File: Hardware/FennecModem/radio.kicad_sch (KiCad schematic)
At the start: 12 parts, among them J201 Conn_Coaxial, U201 DRA818V

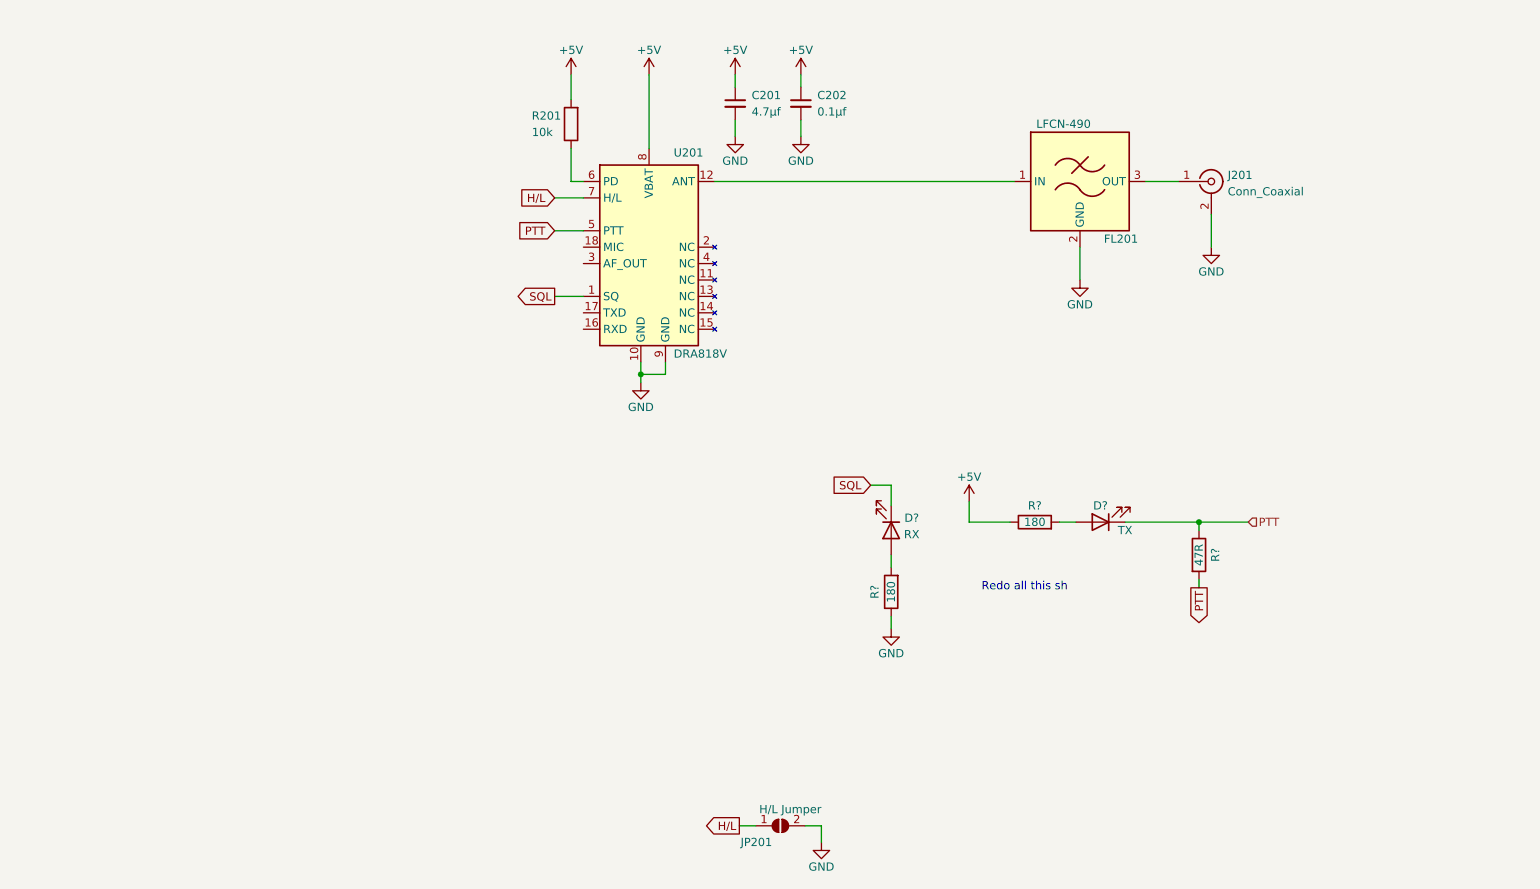
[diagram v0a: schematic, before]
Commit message: Add modem components, bump edge card connector in upstream
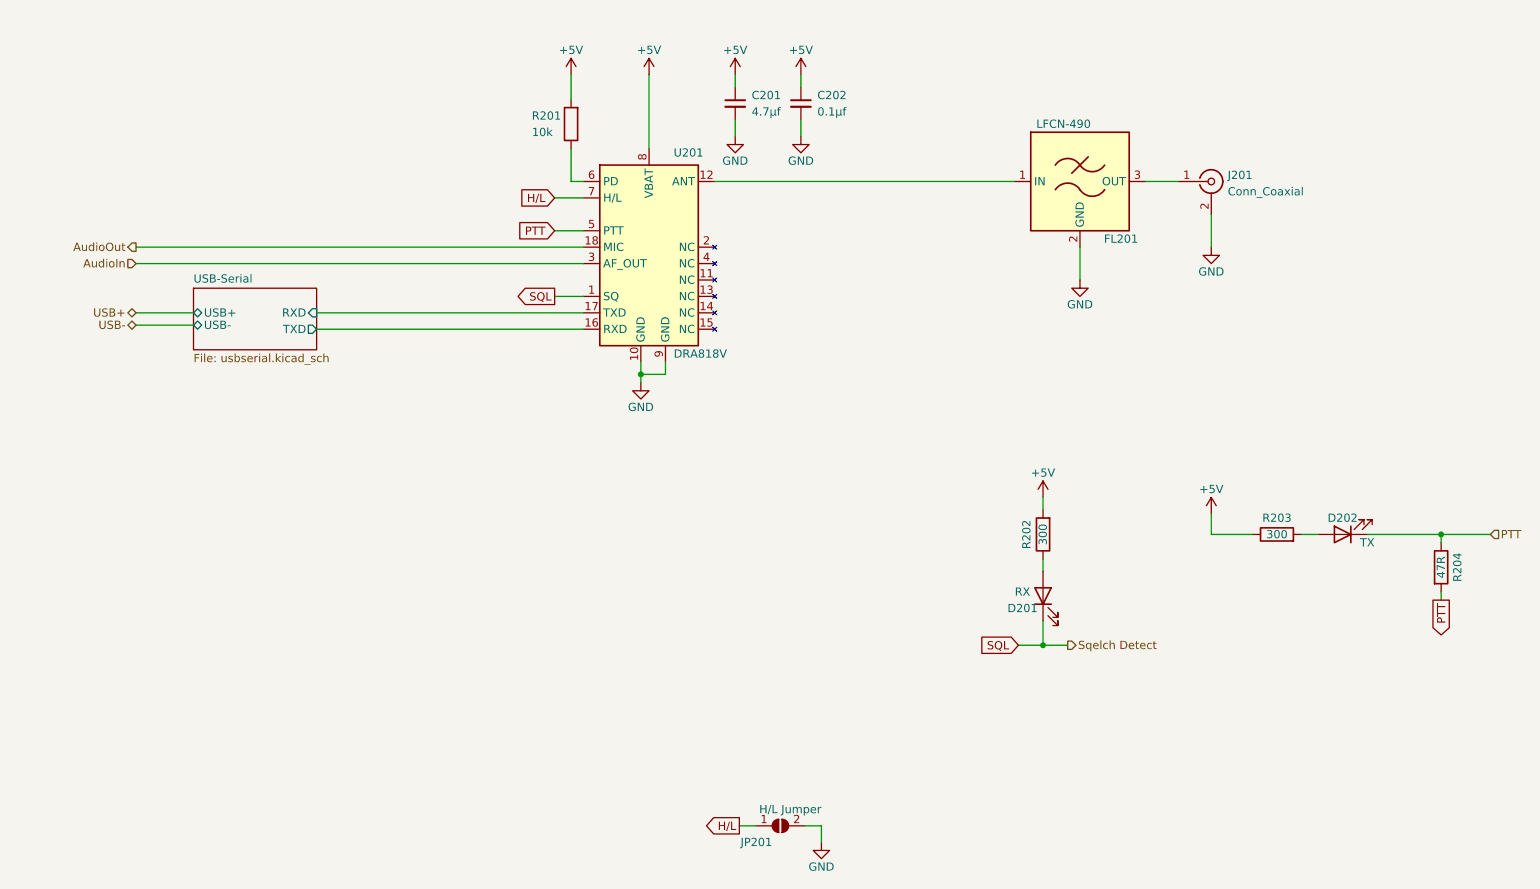
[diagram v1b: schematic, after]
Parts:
- removed D?: RX, LED_SMD:LED_0603_1608Metric, symbol Device:LED
- removed R?: 180, Resistor_SMD:R_0805_2012Metric, symbol Device:R
- added D201: RX, LED_SMD:LED_0603_1608Metric, symbol Device:LED
- added R202: 300, Resistor_SMD:R_0805_2012Metric, symbol Device:R
- R203: renamed from R?; value 180 -> 300
- gave numbers to parts that had none: 2
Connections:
- net +5V: now also R202.2
- net SQL: now also D201.1 (K)
- net USB-Serial/TXD: now reaches U201.16 (RXD)
- net USB-Serial/RXD: now reaches U201.17 (TXD)
- net AudioOut: now reaches U201.18 (MIC)
- net AudioIn: now reaches U201.3 (AF_OUT)
- new net: D201.2 (A), R202.1
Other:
- added sheet USB-Serial (usbserial.kicad_sch)
- note removed: "Redo all this sh"
- moved on the sheet: D202, R203, R204

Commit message: F*ck yeah edge connectors!
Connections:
- net USB-Serial/RXD renamed TXD
- net USB-Serial/TXD renamed RXD
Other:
- removed sheet USB-Serial
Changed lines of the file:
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@@
     (stroke (width 0) (type default) (color 0 0 0 0))
   )
-  (wire (pts (xy 94.615 109.22) (xy 135.89 109.22))
+  (wire (pts (xy 120.015 109.22) (xy 135.89 109.22))
     (stroke (width 0) (type default) (color 0 0 0 0))
   )
@@
     (stroke (width 0) (type default) (color 0 0 0 0))
   )
-  (wire (pts (xy 94.615 111.76) (xy 135.89 111.76))
-    (stroke (width 0) (type default) (color 0 0 0 0))
-  )
-  (wire (pts (xy 66.675 109.22) (xy 75.565 109.22))
+  (wire (pts (xy 120.015 111.76) (xy 135.89 111.76))
     (stroke (width 0) (type default) (color 0 0 0 0))
   )
@@
     (stroke (width 0) (type default) (color 0 0 0 0))
   )
-  (wire (pts (xy 66.675 99.06) (xy 135.89 99.06))
+  (wire (pts (xy 120.015 99.06) (xy 135.89 99.06))
     (stroke (width 0) (type default) (color 0 0 0 0))
   )
@@
     (stroke (width 0) (type default) (color 0 0 0 0))
   )
-  (wire (pts (xy 135.89 101.6) (xy 66.675 101.6))
+  (wire (pts (xy 135.89 101.6) (xy 120.015 101.6))
     (stroke (width 0) (type default) (color 0 0 0 0))
   )
@@
     (stroke (width 0) (type default) (color 0 0 0 0))
   )
-  (wire (pts (xy 66.675 111.125) (xy 75.565 111.125))
-    (stroke (width 0) (type default) (color 0 0 0 0))
-  )
   (wire (pts (xy 247.015 143.51) (xy 249.555 143.51))
     (stroke (width 0) (type default) (color 0 0 0 0))
@@
     )
   )
-  (hierarchical_label "AudioIn" (shape input) (at 66.675 101.6 180)
-    (effects (font (size 1.27 1.27)) (justify right))
-  )
-  (hierarchical_label "AudioOut" (shape output) (at 66.675 99.06 180)
-    (effects (font (size 1.27 1.27)) (justify right))
-  )
-  (hierarchical_label "USB-" (shape bidirectional) (at 66.675 111.125 180)
+  (hierarchical_label "AudioIn" (shape input) (at 120.015 101.6 180)
+    (effects (font (size 1.27 1.27)) (justify right))
+  )
+  (hierarchical_label "AudioOut" (shape output) (at 120.015 99.06 180)
+    (effects (font (size 1.27 1.27)) (justify right))
+  )
+  (hierarchical_label "TXD" (shape output) (at 120.015 109.22 180)
     (effects (font (size 1.27 1.27)) (justify right))
   )
@@
     (effects (font (size 1.27 1.27)) (justify left))
   )
-  (hierarchical_label "USB+" (shape bidirectional) (at 66.675 109.22 180)
-    (effects (font (size 1.27 1.27)) (justify right))
-  )
   (hierarchical_label "Sqelch Detect" (shape output) (at 210.82 160.655 0)
     (effects (font (size 1.27 1.27)) (justify left))
+  )
+  (hierarchical_label "RXD" (shape input) (at 120.015 111.76 180)
+    (effects (font (size 1.27 1.27)) (justify right))
   )
   (symbol (lib_id "power:+5V") (at 169.545 72.39 0) (unit 1)
@@
     (pin "2")
   )
-  (sheet (at 75.565 105.41) (size 19.05 9.525) (fields_autoplaced)
-    (stroke (width 0.1524) (type solid) (color 0 0 0 0))
-    (fill (color 0 0 0 0.0000))
-    (property "Sheet name" "USB-Serial" (id 0) (at 75.565 104.6984 0)
-      (effects (font (size 1.27 1.27)) (justify left bottom))
-    )
-    (property "Sheet file" "usbserial.kicad_sch" (id 1) (at 75.565 115.5196 0)
-      (effects (font (size 1.27 1.27)) (justify left top))
-    )
-    (pin "USB-" bidirectional (at 75.565 111.125 180)
-      (effects (font (size 1.27 1.27)) (justify left))
-    )
-    (pin "USB+" bidirectional (at 75.565 109.22 180)
-      (effects (font (size 1.27 1.27)) (justify left))
-    )
-    (pin "TXD" output (at 94.615 111.76 0)
-      (effects (font (size 1.27 1.27)) (justify right))
-    )
-    (pin "RXD" input (at 94.615 109.22 0)
-      (effects (font (size 1.27 1.27)) (justify right))
-    )
-  )
 )

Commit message: Inital Backplane (#1)
Inital backplane is done, another PR can be opened later for more advanced stuff.
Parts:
- removed JP201: H/L Jumper, Connector_PinHeader_2.54mm:PinHeader_1x02_P2.54mm_Vertical, symbol Jumper:SolderJumper_2_Open
- added D203: TX, LED_THT:LED_D3.0mm_Horizontal_O1.27mm_Z2.0mm, symbol Device:LED
- added D204: TXD, LED_SMD:LED_0805_2012Metric, symbol Device:LED
- added R205: 300, Resistor_SMD:R_0805_2012Metric, symbol Device:R
- added R206: 47R, Resistor_SMD:R_0805_2012Metric, symbol Device:R
- D201: footprint LED_SMD:LED_0603_1608Metric -> LED_THT:LED_D3.0mm_Horizontal_O1.27mm_Z2.0mm
- D202: value TX -> RXD; footprint LED_SMD:LED_0603_1608Metric -> LED_SMD:LED_0805_2012Metric
- R204: value 47R -> 300
- U201: LCSC# (none) -> C3001549
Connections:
- net +5V: now also R203.2, R204.2, R205.2; no longer R203.1
- net PTT: now also D203.1 (K), R206.1; no longer D202.1 (K), R204.1, R204.2, U201.5 (PTT)
- net RXD: now also D202.1 (K)
- net TXD: now also D204.1 (K)
- net Sleep: now reaches R201.1, U201.6 (PD)
- net at D202.2 (A): now also R203.1; no longer R203.2
- net ANT: now reaches FL201.3 (OUT), J201.1 (In)
- net ANT_OUT: now reaches FL201.1 (IN), U201.12 (ANT)
- new net: D203.2 (A), R205.1
- new net: D204.2 (A), R204.1
- new net: R206.2, U201.5 (PTT)
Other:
- note added: "LOW = Sleep HIGH = Normal"
- note added: "Pulldown = 0.5w Float = 1w"
- moved on the sheet: C201, C202, D201, R202

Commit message: Begin laying out and prepping for new tests
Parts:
- added J202: PTT_AMP, Connector_JST:JST_XH_S2B-XH-A-1_1x02_P2.50mm_Horizontal, symbol Connector:Conn_01x02_Pin
- added R207: ?k, Resistor_SMD:R_0805_2012Metric, symbol Device:R
- added U103: PC817, Package_DIP:DIP-4_W7.62mm_SMDSocket_SmallPads, symbol Isolator:PC817
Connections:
- net GND: now also U103.2
- net PTT: now also R207.2
- new net: R207.1, U103.1
- new net: J202.1 (Pin_1), U103.3
- new net: J202.2 (Pin_2), U103.4
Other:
- note added: "Allows us to attach an external amplifier down stream"
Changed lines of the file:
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@@
+    (stroke (width 0) (type default))
+  )
+  (wire (pts (xy 84.455 73.66) (xy 86.36 73.66))
+    (stroke (width 0) (type default))
+  )
+  (wire (pts (xy 84.455 77.47) (xy 84.455 76.2))
+    (stroke (width 0) (type default))
+  )
+  (wire (pts (xy 84.455 76.2) (xy 86.36 76.2))
+    (stroke (width 0) (type default))
+  )
+  (wire (pts (xy 63.5 72.39) (xy 66.675 72.39))
     (stroke (width 0) (type default))
   )
@@
     (stroke (width 0) (type default))
   )
+  (wire (pts (xy 81.915 77.47) (xy 84.455 77.47))
+    (stroke (width 0) (type default))
+  )
   (wire (pts (xy 120.015 91.44) (xy 135.89 91.44))
     (stroke (width 0) (type default))
@@
     (stroke (width 0) (type default))
   )
+  (wire (pts (xy 51.435 72.39) (xy 55.88 72.39))
+    (stroke (width 0) (type default))
+  )
   (wire (pts (xy 234.315 140.335) (xy 234.315 142.24))
     (stroke (width 0) (type default))
@@
     (stroke (width 0) (type default))
   )
+  (wire (pts (xy 64.135 80.645) (xy 64.135 77.47))
+    (stroke (width 0) (type default))
+  )
   (wire (pts (xy 133.985 72.39) (xy 133.985 76.2))
     (stroke (width 0) (type default))
@@
     (stroke (width 0) (type default))
   )
+  (wire (pts (xy 64.135 77.47) (xy 66.675 77.47))
+    (stroke (width 0) (type default))
+  )
   (wire (pts (xy 220.345 159.385) (xy 220.345 163.195))
     (stroke (width 0) (type default))
@@
     (stroke (width 0) (type default))
   )
+  (wire (pts (xy 84.455 72.39) (xy 84.455 73.66))
+    (stroke (width 0) (type default))
+  )
   (wire (pts (xy 144.78 116.84) (xy 144.78 118.745))
     (stroke (width 0) (type default))
   )
+  (wire (pts (xy 81.915 72.39) (xy 84.455 72.39))
+    (stroke (width 0) (type default))
+  )
   (wire (pts (xy 228.6 163.195) (xy 234.315 163.195))
     (stroke (width 0) (type default))
@@
   (wire (pts (xy 133.985 88.9) (xy 135.89 88.9))
     (stroke (width 0) (type default))
+  )
+  (text "Allows us to\nattach an external\namplifier down stream"
+    (at 47.625 69.215 0)
+    (effects (font (size 1.27 1.27)) (justify left bottom))
   )
   (text "Pulldown = 0.5w\nFloat = 1w" (at 106.68 92.71 0)
@@
     (effects (font (size 1.27 1.27)) (justify left bottom))
   )
+  (label "PTT" (at 51.435 72.39 0) (fields_autoplaced)
+    (effects (font (size 1.27 1.27)) (justify left bottom))
+  )
   (label "PTT" (at 199.39 163.195 0) (fields_autoplaced)
     (effects (font (size 1.27 1.27)) (justify left bottom))
@@
     )
   )
+  (symbol (lib_id "power:GND") (at 64.135 80.645 0) (unit 1)
+    (in_bom yes) (on_board yes) (dnp no)
+    (property "Reference" "#PWR0204" (at 64.135 86.995 0)
+      (effects (font (size 1.27 1.27)) hide)
+    )
+    (property "Value" "GND" (at 64.135 84.455 0)
+      (effects (font (size 1.27 1.27)))
+    )
+    (property "Footprint" "" (at 64.135 80.645 0)
+      (effects (font (size 1.27 1.27)) hide)
+    )
+    (property "Datasheet" "" (at 64.135 80.645 0)
+      (effects (font (size 1.27 1.27)) hide)
+    )
+    (pin "1")
+    (instances
+      (project "FennecModem"
+        (path "/8cb1f8f8-0f28-4c6f-8a0b-e6b064917aa9/cf3d0f33-271b-4df1-9d86-6d97bc01010a"
+          (reference "#PWR0204") (unit 1)
+        )
+      )
+    )
+  )
   (symbol (lib_id "power:+5V") (at 220.345 140.335 0) (unit 1)
     (in_bom yes) (on_board yes) (dnp no)
@@
     )
   )
+  (symbol (lib_id "Device:R") (at 59.69 72.39 270) (unit 1)
+    (in_bom yes) (on_board yes) (dnp no)
+    (property "Reference" "R207" (at 59.69 74.93 90)
+      (effects (font (size 1.27 1.27)))
+    )
+    (property "Value" "?k" (at 59.69 76.835 90)
+      (effects (font (size 1.27 1.27)))
+    )
+    (property "Footprint" "Resistor_SMD:R_0805_2012Metric" (at 59.69 70.612 90)
+      (effects (font (size 1.27 1.27)) hide)
+    )
+    (property "Datasheet" "~" (at 59.69 72.39 0)
+      (effects (font (size 1.27 1.27)) hide)
+    )
+    (pin "1")
+    (pin "2")
+    (instances
+      (project "FennecModem"
+        (path "/8cb1f8f8-0f28-4c6f-8a0b-e6b064917aa9/cf3d0f33-271b-4df1-9d86-6d97bc01010a"
+          (reference "R207") (unit 1)
+        )
+      )
+    )
+  )
   (symbol (lib_id "power:+5V") (at 146.05 72.39 0) (unit 1)
     (in_bom yes) (on_board yes) (dnp no)
@@
         (path "/8cb1f8f8-0f28-4c6f-8a0b-e6b064917aa9/cf3d0f33-271b-4df1-9d86-6d97bc01010a"
           (reference "R202") (unit 1)
+        )
+      )
+    )
+  )
+  (symbol (lib_id "Isolator:PC817") (at 74.295 74.93 0) (unit 1)
+    (in_bom yes) (on_board yes) (dnp no) (fields_autoplaced)
+    (property "Reference" "U103" (at 74.295 66.675 0)
+      (effects (font (size 1.27 1.27)))
+    )
+    (property "Value" "PC817" (at 74.295 69.215 0)
+      (effects (font (size 1.27 1.27)))
+    )
+    (property "Footprint" "Package_DIP:DIP-4_W7.62mm_SMDSocket_SmallPads" (at 69.215 80.01 0)
+      (effects (font (size 1.27 1.27) italic) (justify left) hide)
+    )
+    (property "Datasheet" "http://www.soselectronic.cz/a_info/resource/d/pc817.pdf" (at 74.295 74.93 0)
+      (effects (font (size 1.27 1.27)) (justify left) hide)
+    )
+    (property "LCSC#" "C3025164" (at 74.295 74.93 0)
+      (effects (font (size 1.27 1.27)) hide)
+    )
+    (pin "3")
+    (pin "1")
+    (pin "4")
+    (pin "2")
+    (instances
+      (project "FennecModem"
+        (path "/8cb1f8f8-0f28-4c6f-8a0b-e6b064917aa9"
+          (reference "U103") (unit 1)
+        )
+        (path "/8cb1f8f8-0f28-4c6f-8a0b-e6b064917aa9/cf3d0f33-271b-4df1-9d86-6d97bc01010a"
+          (reference "U202") (unit 1)
         )
       )
@@
         )
       )
+    )
+  )
+  (symbol (lib_id "Connector:Conn_01x02_Pin") (at 91.44 76.2 180) (unit 1)
+    (in_bom yes) (on_board yes) (dnp no) (fields_autoplaced)
+    (property "Reference" "J202" (at 92.71 73.66 0)
+      (effects (font (size 1.27 1.27)) (justify right))
+    )
+    (property "Value" "PTT_AMP" (at 92.71 76.2 0)
+      (effects (font (size 1.27 1.27)) (justify right))
+    )
+    (property "Footprint" "Connector_JST:JST_XH_S2B-XH-A-1_1x02_P2.50mm_Horizontal" (at 91.44 76.2 0)
+      (effects (font (size 1.27 1.27)) hide)
+    )
+    (property "Datasheet" "~" (at 91.44 76.2 0)
+      (effects (font (size 1.27 1.27)) hide)
+    )
+    (pin "1")
+    (pin "2")
+    (instances
+      (project "FennecModem"
+        (path "/8cb1f8f8-0f28-4c6f-8a0b-e6b064917aa9/cf3d0f33-271b-4df1-9d86-6d97bc01010a"
+          (reference "J202") (unit 1)
+        )
+      )

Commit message: Include new chip! 3v3 system from now on..
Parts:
- renumbered U103 to U202
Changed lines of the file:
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@@
   (symbol (lib_id "Isolator:PC817") (at 74.295 74.93 0) (unit 1)
     (in_bom yes) (on_board yes) (dnp no) (fields_autoplaced)
-    (property "Reference" "U103" (at 74.295 66.675 0)
+    (property "Reference" "U202" (at 74.295 66.675 0)
       (effects (font (size 1.27 1.27)))
     )
@@
     (instances
       (project "FennecModem"
-        (path "/8cb1f8f8-0f28-4c6f-8a0b-e6b064917aa9"
-          (reference "U103") (unit 1)
-        )
         (path "/8cb1f8f8-0f28-4c6f-8a0b-e6b064917aa9/cf3d0f33-271b-4df1-9d86-6d97bc01010a"
           (reference "U202") (unit 1)
